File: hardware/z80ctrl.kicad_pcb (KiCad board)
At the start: 2 copper layers, 99.8 x 49.9 mm, 28 parts, among them J1 BUS, J2 BUSEXT, J4 IOADDR, J5 SERIAL1, J6 SERIAL2, J7 SD, SW1 RESET, SW2 HALT, U1 74HCT139, U2 ATMEGA1284P-PU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

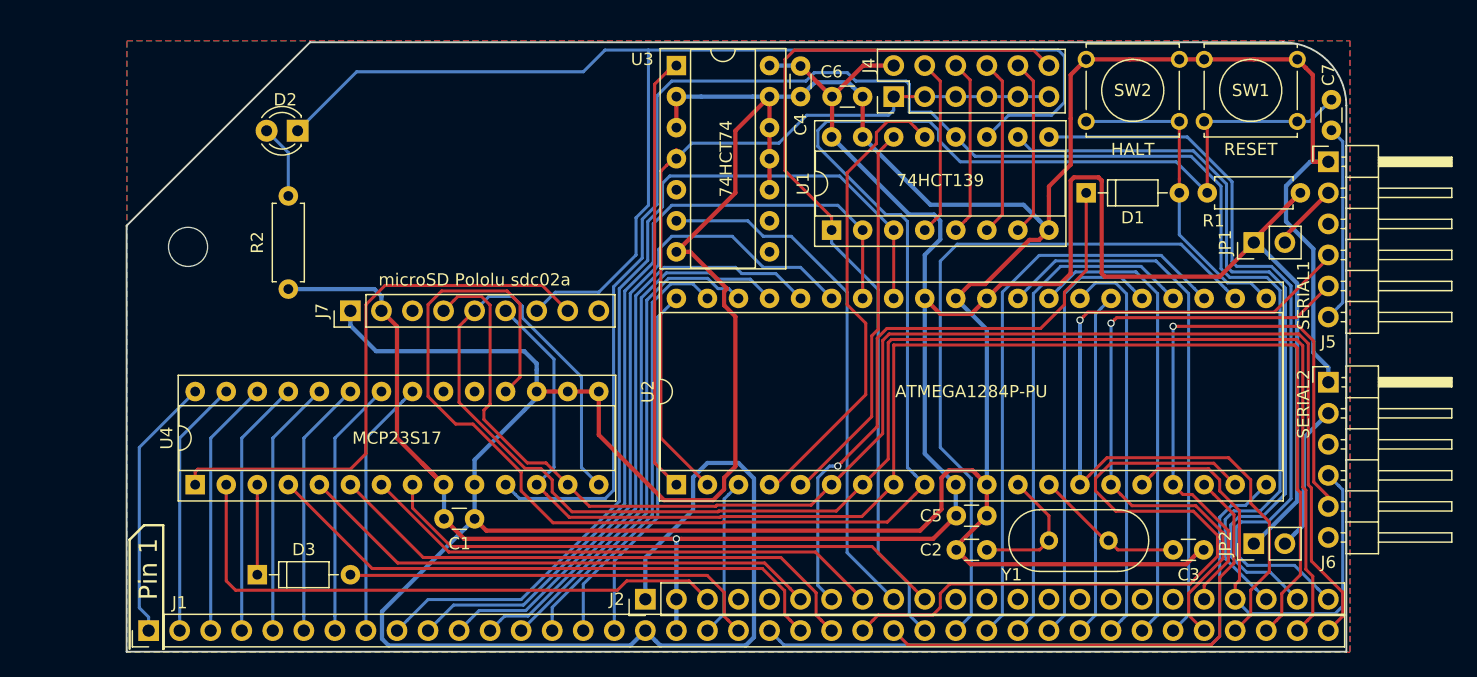
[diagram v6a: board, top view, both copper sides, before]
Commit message: Reroute SPI tracks, cleanup track layout
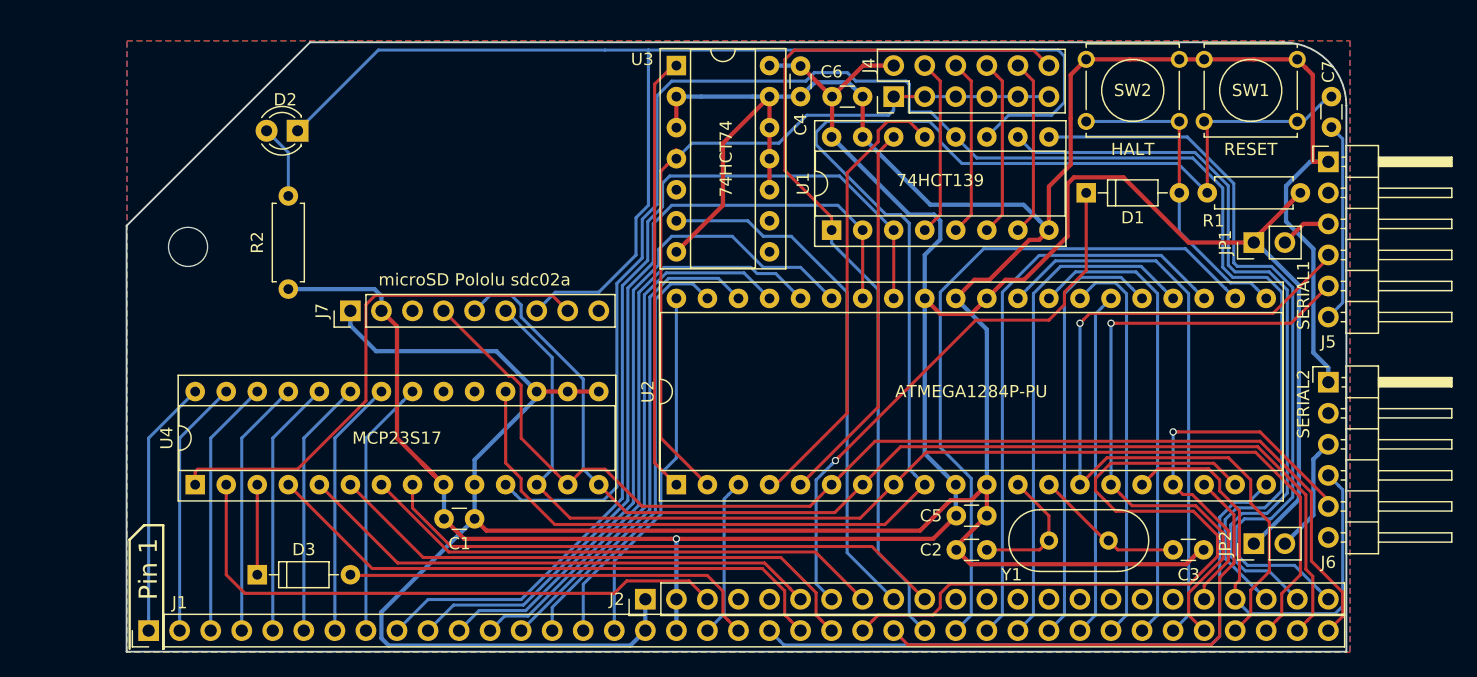
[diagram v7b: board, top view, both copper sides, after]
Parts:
- C2: value 22pf -> 18pf
- C3: value 20pf -> 18pf
- moved C7 0.25 mm to (252.5, 110.5)
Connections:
- JP1 pad 2: Net-(J5-Pad2) -> Net-(J5-Pad3)
- JP2 pad 2: Net-(J6-Pad2) -> Net-(J6-Pad3)
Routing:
- net GND: track 381.1 -> 300.5 mm
- net MISO: track 139.1 -> 96.5 mm
- net /AVRRST: track 156.2 -> 129.7 mm
- net MOSI: track 120.3 -> 98.0 mm
- net SCK: track 116.8 -> 95.8 mm
- net TX2: track 51.3 -> 32.2 mm
- net RX: track 79.0 -> 65.3 mm
- net Net-(J6-Pad2): track 12.1 -> 0.00 mm
- net Net-(J6-Pad3): track 0.00 -> 9.60 mm
- net VCC: track 215.3 -> 206.7 mm
- net Net-(J5-Pad2): track 6.55 -> 1.02 mm
- net Net-(J5-Pad3): track 0.00 -> 4.70 mm
- net /HALT: track 50.6 -> 46.4 mm
- net /SDCD: track 46.4 -> 43.2 mm
- net D0: track 58.3 -> 56.6 mm
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
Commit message: Reroute DTR trace away from board edge to avoid manufacturing defects
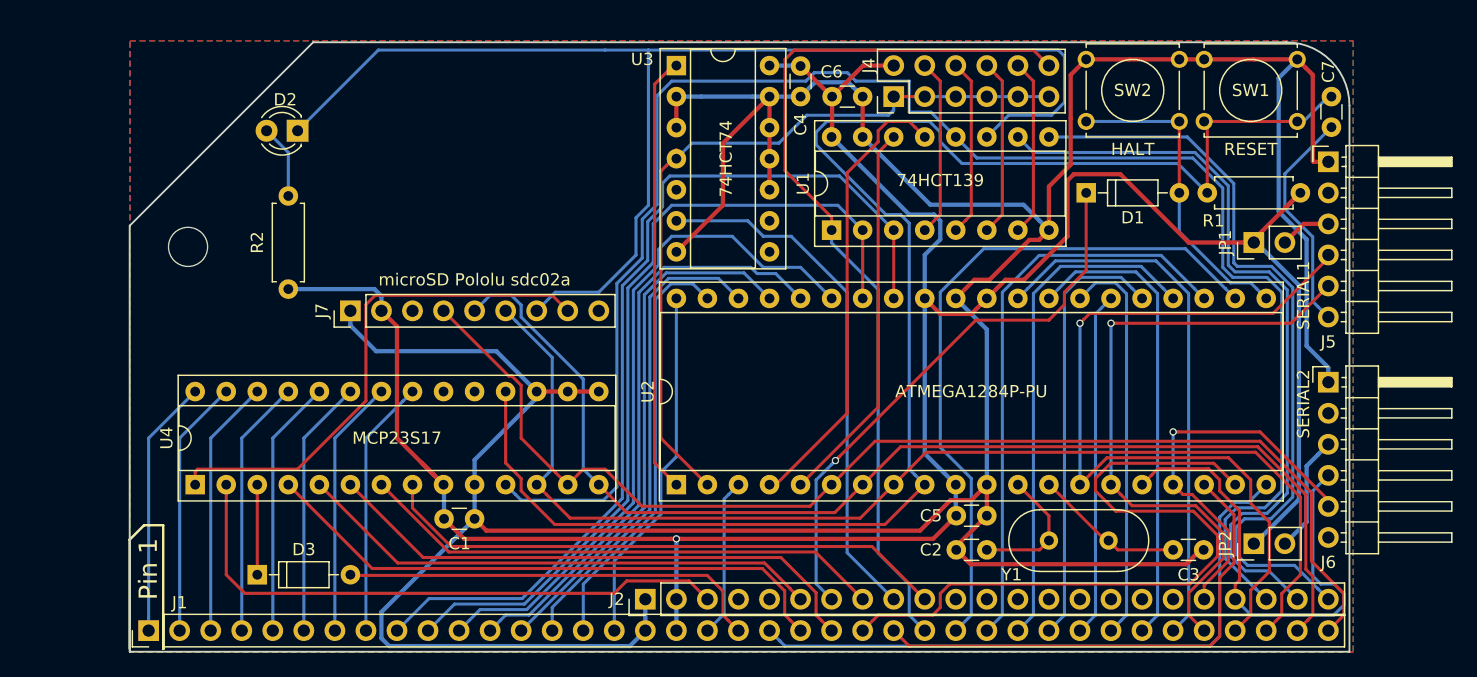
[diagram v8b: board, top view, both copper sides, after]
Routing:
- net GND: track 300.5 -> 307.5 mm
- net Net-(C7-Pad1): track 16.3 -> 18.8 mm
- net RX2: track 38.6 -> 40.5 mm
